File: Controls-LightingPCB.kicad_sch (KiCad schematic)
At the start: 88 parts, among them J1 MinionConn, Q1 2N7000, Q2 2N7000, Q3 2N7000, Q4 2N7000, Q5 2N7000, U1 NCP1117-3.3_SOT223

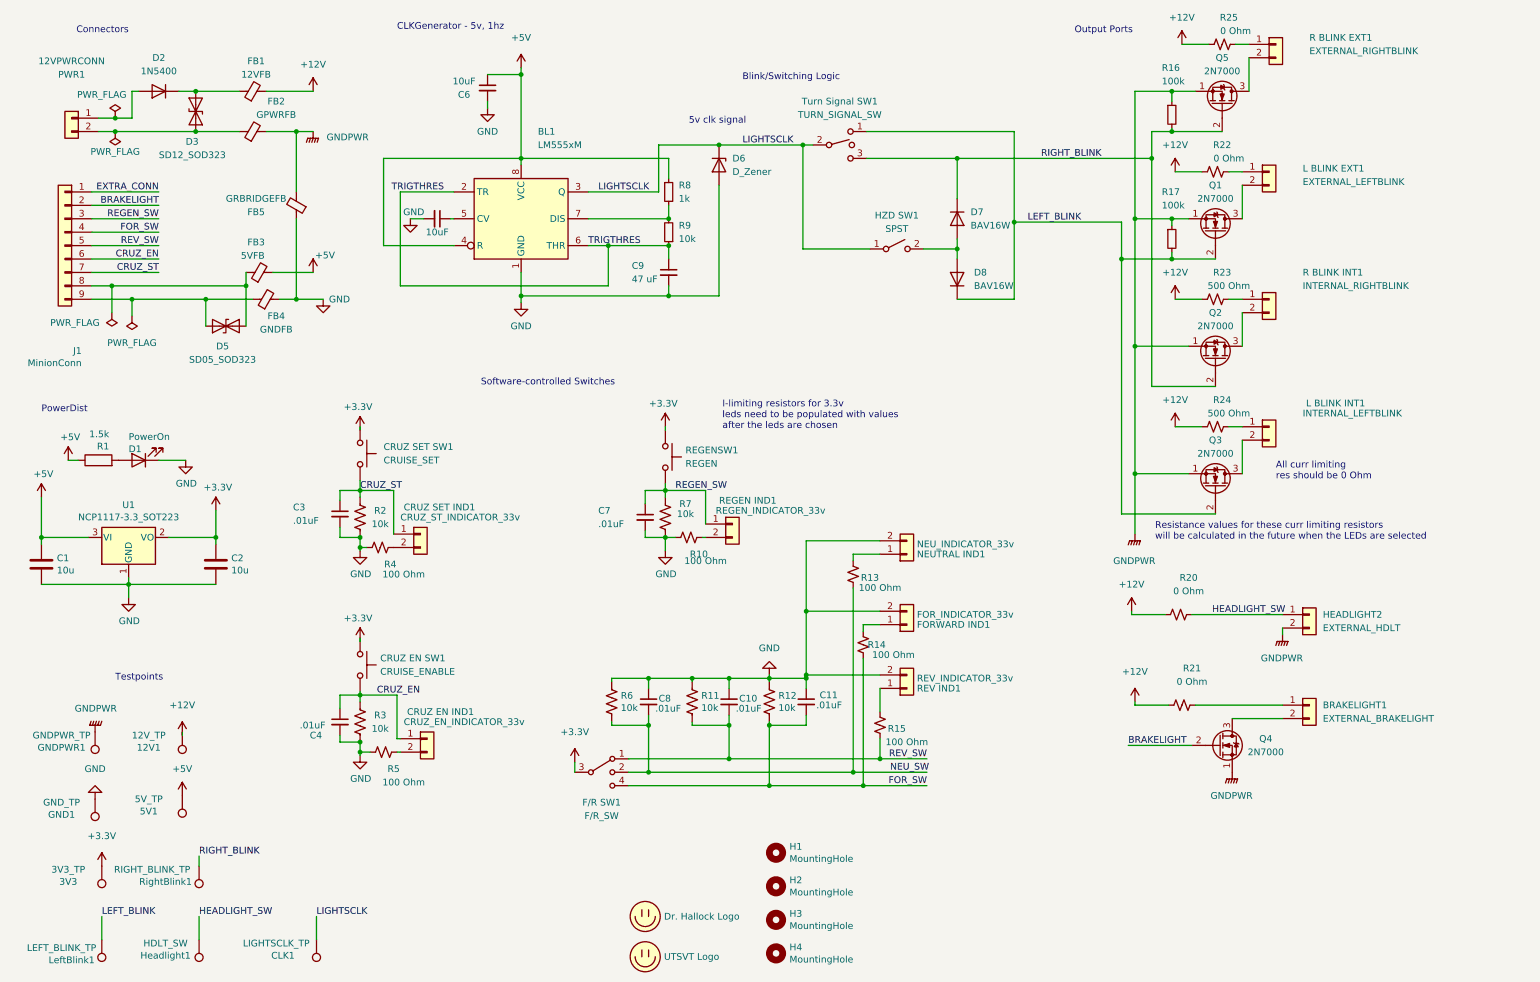
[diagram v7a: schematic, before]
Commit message: schematic fixes and minor changes. no major part changes
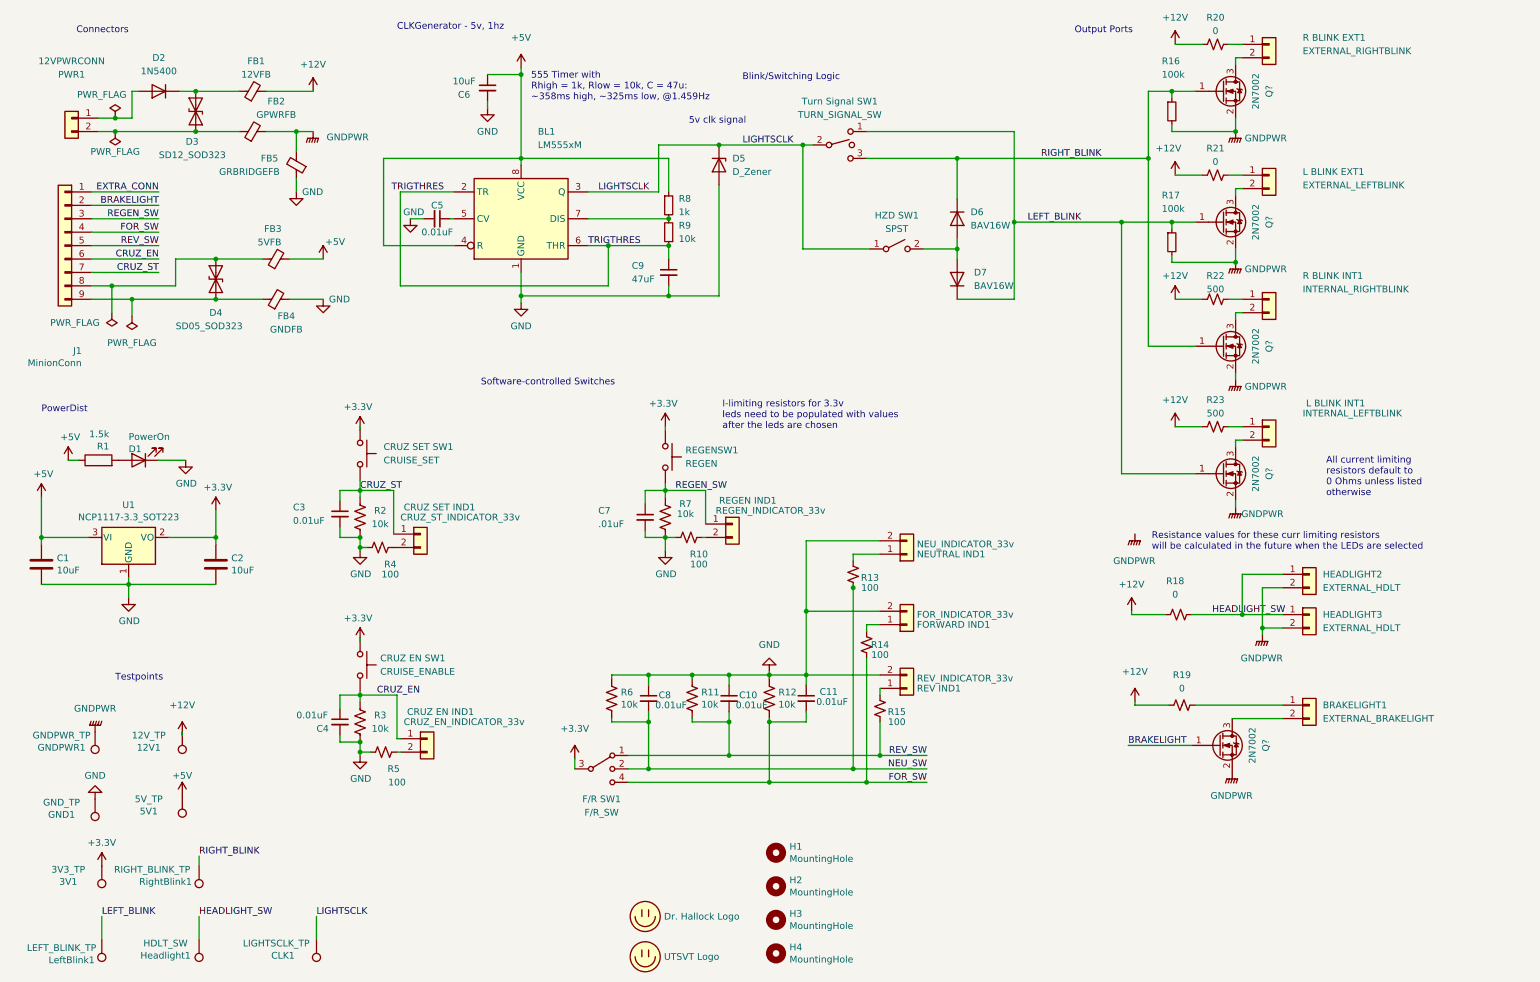
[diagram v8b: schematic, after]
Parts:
- removed Q1, Q2, Q3, Q4, Q5: 2N7000, Package_TO_SOT_SMD:SOT-23, symbol Transistor_FET:2N7000
- added HEADLIGHT2: EXTERNAL_HDLT, Connector_Molex:Molex_Micro-Fit_3.0_43650-0215_1x02_P3.00mm_Vertical, symbol Connector_Generic:Conn_01x02
- added Q? (x5): 2N7002, Package_TO_SOT_SMD:SOT-23, symbol Transistor_FET:2N7002
- C1, C2: value 10u -> 10uF
- C10, C11, C3, C4, C8: value .01uF -> 0.01uF
- C5: value 10uF -> 0.01uF
- C9: value 47 uF -> 47uF
- R10, R13, R14, R15, R4, R5: value 100 Ohm -> 100
- R18: renamed from R20; value 0 Ohm -> 0
- R19: renamed from R21; value 0 Ohm -> 0
- R20: renamed from R25; value 0 Ohm -> 0
- R21: renamed from R22; value 0 Ohm -> 0
- R22: renamed from R23; value 500 Ohm -> 500
- R23: renamed from R24; value 500 Ohm -> 500
- renumbered 3V3 to 3V1, D5 to D4, D6 to D5, D7 to D6, D8 to D7, HEADLIGHT2 to HEADLIGHT3
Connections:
- net BRAKELIGHT: now also Q?.1 (G)
- net GNDPWR: now also R16.2, R17.2, HEADLIGHT2.2 (Pin_2), Q?.2 (S), Q?.2 (S), Q?.2 (S), Q?.2 (S), Q?.2 (S); no longer R16.1, R17.1
- net HEADLIGHT_SW: now also HEADLIGHT2.1 (Pin_1)
- net LEFT_BLINK: now also R17.1, Q?.1 (G), Q?.1 (G); no longer R17.2
- net RIGHT_BLINK: now also R16.1, Q?.1 (G), Q?.1 (G); no longer R16.2
- net at FB3.1, J1.8 (Pin_8): now also D4.1 (A1); no longer D4.2 (A2)
- net at FB4.1, J1.9 (Pin_9): now also D4.2 (A2); no longer D4.1 (A1)
- net at BRAKELIGHT1.2 (Pin_2): now also Q?.3 (D)
- net at L BLINK INT1.2 (Pin_2): now also Q?.3 (D)
- net at L BLINK EXT1.2 (Pin_2): now also Q?.3 (D)
- net at R BLINK EXT1.2 (Pin_2): now also Q?.3 (D)
- net at R BLINK INT1.2 (Pin_2): now also Q?.3 (D)
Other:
- note added: "555 Timer with Rhigh = 1k, Rlow = 10k, C = 47u: ~358ms high, ~325ms low, @1.459Hz"
- note added: "All current limiting resistors default to 0 Ohms unless listed otherwise"
- note removed: "All curr limiting res should be 0 Ohm"
- moved on the sheet: C10, C11, C8, D4, F/R SW1, FB3, FB4, FB5, L BLINK EXT1, R BLINK EXT1, R11, R12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
